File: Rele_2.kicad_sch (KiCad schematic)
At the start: 6 parts, among them J16 Rele_2, J33 Pin GND, K5 SRD-05VDC-SL-C, Q13 PMBT3904,235

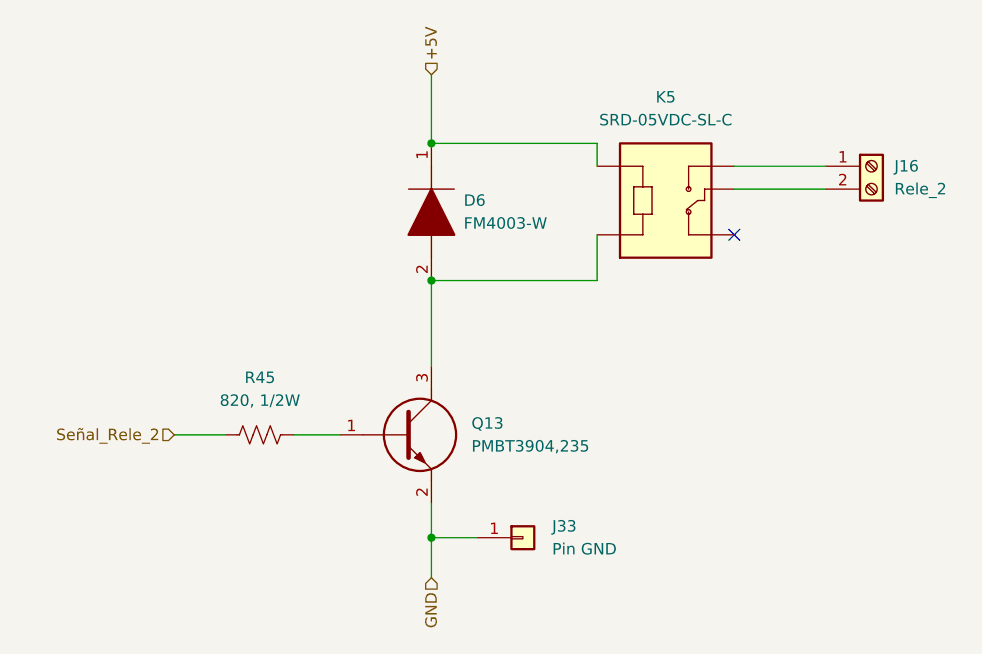
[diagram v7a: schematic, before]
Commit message: Se modificaron algunos componentes, según disponibilidad
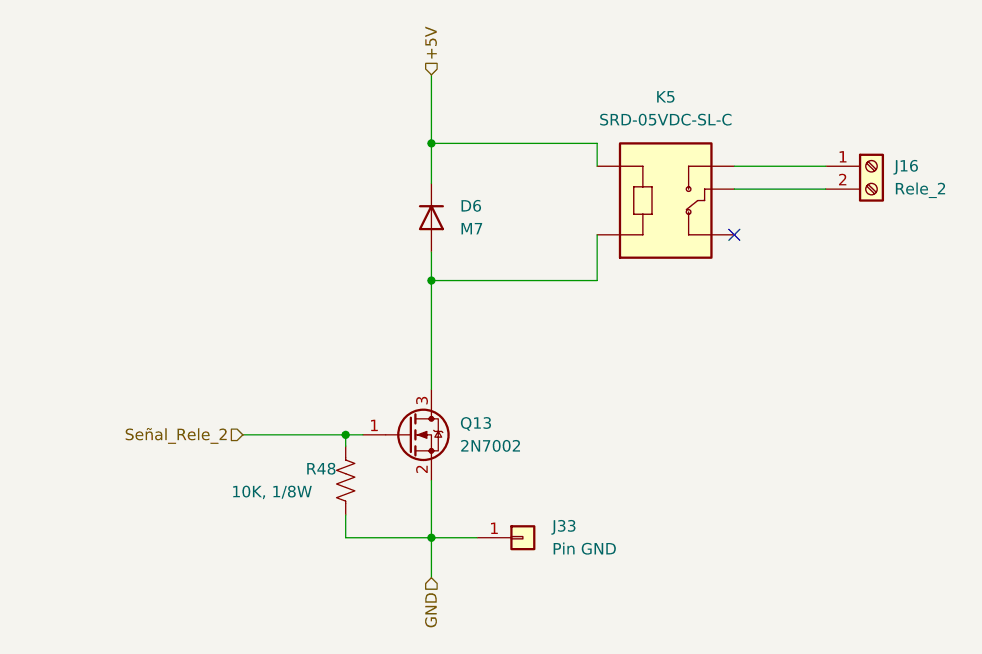
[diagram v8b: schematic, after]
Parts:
- removed D6: FM4003-W, FM4003W:DIOM5025X231N, symbol FM4003-W:FM4003-W
- removed Q13: PMBT3904,235, PMBT3904,235:SOT95P230X110-3N, symbol PMBT3904,235:PMBT3904,235
- removed R45: 820, 1/2W, Resistor_SMD:R_0805_2012Metric, symbol Device:R_US
- added D6: M7, Diode_SMD:D_SMA, symbol Device:D
- added Q13: 2N7002, Package_TO_SOT_SMD:SOT-23, symbol Transistor_FET:2N7002
- added R48: 10K, 1/8W, Resistor_SMD:R_0805_2012Metric, symbol Device:R_US
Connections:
- net +5V: now also D6.1 (K)
- net GND: now also Q13.2 (S), R48.2
- net Señal_Rele_2: now also Q13.1 (G), R48.1
- net at K5.A2: now also D6.2 (A), Q13.3 (D)
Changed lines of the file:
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@@
 (kicad_sch (version 20211123) (generator eeschema)
   (paper "A4")
+  (junction (at 139.065 72.39) (diameter 0) (color 0 0 0 0)
+  )
   (junction (at 139.065 116.205) (diameter 0) (color 0 0 0 0)
   )
-  (junction (at 139.065 72.39) (diameter 0) (color 0 0 0 0)
+  (junction (at 129.54 104.775) (diameter 0) (color 0 0 0 0)
   )
   (junction (at 139.065 87.63) (diameter 0) (color 0 0 0 0)
   )
   (no_connect (at 172.72 82.55))
+  (wire (pts (xy 129.54 113.665) (xy 129.54 116.205))
+    (stroke (width 0) (type default) (color 0 0 0 0))
+  )
   (wire (pts (xy 139.065 72.39) (xy 157.48 72.39))
     (stroke (width 0) (type default) (color 0 0 0 0))
@@
     (stroke (width 0) (type default) (color 0 0 0 0))
   )
+  (wire (pts (xy 129.54 104.775) (xy 129.54 106.045))
+    (stroke (width 0) (type default) (color 0 0 0 0))
+  )
+  (wire (pts (xy 129.54 116.205) (xy 139.065 116.205))
+    (stroke (width 0) (type default) (color 0 0 0 0))
+  )
   (wire (pts (xy 157.48 87.63) (xy 157.48 82.55))
+    (stroke (width 0) (type default) (color 0 0 0 0))
+  )
+  (wire (pts (xy 129.54 104.775) (xy 131.445 104.775))
     (stroke (width 0) (type default) (color 0 0 0 0))
   )
@@
     (stroke (width 0) (type default) (color 0 0 0 0))
   )
-  (wire (pts (xy 139.065 87.63) (xy 139.065 97.155))
+  (wire (pts (xy 139.065 87.63) (xy 139.065 99.695))
     (stroke (width 0) (type default) (color 0 0 0 0))
   )
@@
     (stroke (width 0) (type default) (color 0 0 0 0))
   )
-  (wire (pts (xy 139.065 112.395) (xy 139.065 116.205))
+  (wire (pts (xy 139.065 72.39) (xy 139.065 76.835))
+    (stroke (width 0) (type default) (color 0 0 0 0))
+  )
+  (wire (pts (xy 139.065 109.855) (xy 139.065 116.205))
+    (stroke (width 0) (type default) (color 0 0 0 0))
+  )
+  (wire (pts (xy 139.065 84.455) (xy 139.065 87.63))
     (stroke (width 0) (type default) (color 0 0 0 0))
   )
@@
     (stroke (width 0) (type default) (color 0 0 0 0))
   )
-  (wire (pts (xy 110.49 104.775) (xy 116.205 104.775))
+  (wire (pts (xy 118.11 104.775) (xy 129.54 104.775))
     (stroke (width 0) (type default) (color 0 0 0 0))
   )
-  (wire (pts (xy 123.825 104.775) (xy 128.905 104.775))
-    (stroke (width 0) (type default) (color 0 0 0 0))
-  )
-  (hierarchical_label "Señal_Rele_2" (shape input) (at 110.49 104.775 180)
+  (hierarchical_label "Señal_Rele_2" (shape input) (at 118.11 104.775 180)
     (effects (font (size 1.27 1.27)) (justify right))
   )
@@
     (effects (font (size 1.27 1.27)) (justify left))
   )
-  (symbol (lib_id "FM4003-W:FM4003-W") (at 139.065 72.39 270) (unit 1)
-    (in_bom yes) (on_board yes) (fields_autoplaced)
-    (property "Reference" "D6" (id 0) (at 142.6464 78.7399 90)
+  (symbol (lib_id "Device:R_US") (at 129.54 109.855 0) (unit 1)
+    (in_bom yes) (on_board yes)
+    (property "Reference" "R48" (id 0) (at 125.095 108.585 0)
       (effects (font (size 1.27 1.27)) (justify left))
     )
-    (property "Value" "FM4003-W" (id 1) (at 142.6464 81.2799 90)
+    (property "Value" "10K, 1/8W" (id 1) (at 116.84 111.125 0)
       (effects (font (size 1.27 1.27)) (justify left))
     )
-    (property "Footprint" "FM4003W:DIOM5025X231N" (id 2) (at 139.065 83.82 0)
-      (effects (font (size 1.27 1.27)) (justify left) hide)
+    (property "Footprint" "Resistor_SMD:R_0805_2012Metric" (id 2) (at 130.556 110.109 90)
+      (effects (font (size 1.27 1.27)) hide)
     )
-    (property "Datasheet" "https://componentsearchengine.com/Datasheets/1/FM4003-W.pdf" (id 3) (at 136.525 83.82 0)
-      (effects (font (size 1.27 1.27)) (justify left) hide)
-    )
-    (property "Description" "Rectifiers 1A 200V GP" (id 4) (at 133.985 83.82 0)
-      (effects (font (size 1.27 1.27)) (justify left) hide)
-    )
-    (property "Height" "2.31" (id 5) (at 131.445 83.82 0)
-      (effects (font (size 1.27 1.27)) (justify left) hide)
-    )
-    (property "Manufacturer_Name" "Rectron" (id 6) (at 128.905 83.82 0)
-      (effects (font (size 1.27 1.27)) (justify left) hide)
-    )
-    (property "Manufacturer_Part_Number" "FM4003-W" (id 7) (at 126.365 83.82 0)
-      (effects (font (size 1.27 1.27)) (justify left) hide)
-    )
-    (property "Mouser Part Number" "583-FM4003-W" (id 8) (at 123.825 83.82 0)
-      (effects (font (size 1.27 1.27)) (justify left) hide)
-    )
-    (property "Mouser Price/Stock" "https://www.mouser.co.uk/ProductDetail/Rectron/FM4003-W/?qs=5h8Q3Z7TNRlJu6QU92Ho0w%3D%3D" (id 9) (at 121.285 83.82 0)
-      (effects (font (size 1.27 1.27)) (justify left) hide)
-    )
-    (property "Arrow Part Number" "FM4003-W" (id 10) (at 118.745 83.82 0)
-      (effects (font (size 1.27 1.27)) (justify left) hide)
-    )
-    (property "Arrow Price/Stock" "https://www.arrow.com/en/products/fm4003-w/rectron" (id 11) (at 116.205 83.82 0)
-      (effects (font (size 1.27 1.27)) (justify left) hide)
-    )
-    (property "Mouser Testing Part Number" "" (id 12) (at 113.665 83.82 0)
-      (effects (font (size 1.27 1.27)) (justify left) hide)
-    )
-    (property "Mouser Testing Price/Stock" "" (id 13) (at 111.125 83.82 0)
-      (effects (font (size 1.27 1.27)) (justify left) hide)
+    (property "Datasheet" "~" (id 3) (at 129.54 109.855 0)
+      (effects (font (size 1.27 1.27)) hide)
     )
     (pin "1")
@@
     )
     (property "Datasheet" "~" (id 3) (at 187.96 74.93 0)
+      (effects (font (size 1.27 1.27)) hide)
+    )
+    (pin "1")
+    (pin "2")
+  )
+  (symbol (lib_id "Device:D") (at 139.065 80.645 270) (unit 1)
+    (in_bom yes) (on_board yes) (fields_autoplaced)
+    (property "Reference" "D6" (id 0) (at 142.24 79.3749 90)
+      (effects (font (size 1.27 1.27)) (justify left))
+    )
+    (property "Value" "M7" (id 1) (at 142.24 81.9149 90)
+      (effects (font (size 1.27 1.27)) (justify left))
+    )
+    (property "Footprint" "Diode_SMD:D_SMA" (id 2) (at 139.065 80.645 0)
+      (effects (font (size 1.27 1.27)) hide)
+    )
+    (property "Datasheet" "~" (id 3) (at 139.065 80.645 0)
       (effects (font (size 1.27 1.27)) hide)
     )
@@
     (pin "NO")
   )
-  (symbol (lib_id "PMBT3904,235:PMBT3904,235") (at 128.905 104.775 0) (unit 1)
+  (symbol (lib_id "Transistor_FET:2N7002") (at 136.525 104.775 0) (unit 1)
     (in_bom yes) (on_board yes) (fields_autoplaced)
-    (property "Reference" "Q13" (id 0) (at 143.51 103.5049 0)
+    (property "Reference" "Q13" (id 0) (at 142.24 103.5049 0)
       (effects (font (size 1.27 1.27)) (justify left))
     )
-    (property "Value" "PMBT3904,235" (id 1) (at 143.51 106.0449 0)
+    (property "Value" "2N7002" (id 1) (at 142.24 106.0449 0)
       (effects (font (size 1.27 1.27)) (justify left))
     )
-    (property "Footprint" "PMBT3904,235:SOT95P230X110-3N" (id 2) (at 142.875 108.585 0)
-      (effects (font (size 1.27 1.27)) (justify left) hide)
+    (property "Footprint" "Package_TO_SOT_SMD:SOT-23" (id 2) (at 141.605 106.68 0)
+      (effects (font (size 1.27 1.27) italic) (justify left) hide)
     )
-    (property "Datasheet" "https://assets.nexperia.com/documents/data-sheet/PMBT3904.pdf" (id 3) (at 142.875 111.125 0)
-      (effects (font (size 1.27 1.27)) (justify left) hide)
-    )
-    (property "Description" "PMBT3904 - NPN switching transistor" (id 4) (at 142.875 113.665 0)
-      (effects (font (size 1.27 1.27)) (justify left) hide)
-    )
-    (property "Height" "1.1" (id 5) (at 142.875 116.205 0)
-      (effects (font (size 1.27 1.27)) (justify left) hide)
-    )
-    (property "Manufacturer_Name" "Nexperia" (id 6) (at 142.875 118.745 0)
-      (effects (font (size 1.27 1.27)) (justify left) hide)
-    )
-    (property "Manufacturer_Part_Number" "PMBT3904,235" (id 7) (at 142.875 121.285 0)
-      (effects (font (size 1.27 1.27)) (justify left) hide)
-    )
-    (property "Mouser Part Number" "771-PMBT3904235" (id 8) (at 142.875 123.825 0)
-      (effects (font (size 1.27 1.27)) (justify left) hide)
-    )
-    (property "Mouser Price/Stock" "https://www.mouser.co.uk/ProductDetail/Nexperia/PMBT3904235?qs=LOCUfHb8d9uziIfl4fmvZg%3D%3D" (id 9) (at 142.875 126.365 0)
-      (effects (font (size 1.27 1.27)) (justify left) hide)
-    )
-    (property "Arrow Part Number" "PMBT3904,235" (id 10) (at 142.875 128.905 0)
-      (effects (font (size 1.27 1.27)) (justify left) hide)
-    )
-    (property "Arrow Price/Stock" "https://www.arrow.com/en/products/pmbt3904235/nexperia?region=nac" (id 11) (at 142.875 131.445 0)
-      (effects (font (size 1.27 1.27)) (justify left) hide)
-    )
-    (property "Mouser Testing Part Number" "" (id 12) (at 142.875 133.985 0)
-      (effects (font (size 1.27 1.27)) (justify left) hide)
-    )
-    (property "Mouser Testing Price/Stock" "" (id 13) (at 142.875 136.525 0)
+    (property "Datasheet" "https://www.onsemi.com/pub/Collateral/NDS7002A-D.PDF" (id 3) (at 136.525 104.775 0)
       (effects (font (size 1.27 1.27)) (justify left) hide)
     )
@@
     (pin "3")
   )
-  (symbol (lib_id "Device:R_US") (at 120.015 104.775 90) (unit 1)
-    (in_bom yes) (on_board yes) (fields_autoplaced)
-    (property "Reference" "R45" (id 0) (at 120.015 98.425 90))
-    (property "Value" "820, 1/2W" (id 1) (at 120.015 100.965 90))
-    (property "Footprint" "Resistor_SMD:R_0805_2012Metric" (id 2) (at 120.269 103.759 90)
-      (effects (font (size 1.27 1.27)) hide)
-    )
-    (property "Datasheet" "~" (id 3) (at 120.015 104.775 0)
-      (effects (font (size 1.27 1.27)) hide)
-    )
-    (pin "1")
-    (pin "2")
-  )
 )
